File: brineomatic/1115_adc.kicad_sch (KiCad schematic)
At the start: 4 parts, among them U1 ADS1015IDGS

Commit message: getting closer.  added tds
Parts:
- removed U1: ADS1015IDGS, Package_SO:TSSOP-10_3x3mm_P0.5mm, symbol Analog_ADC:ADS1015IDGS
- added R20, R21: 2.2k, Resistor_SMD:R_0805_2012Metric_Pad1.20x1.40mm_HandSolder, symbol Device:R_Small_US
- added U6: ADS1115IDGS, Package_SO:TSSOP-10_3x3mm_P0.5mm, symbol Analog_ADC:ADS1115IDGS
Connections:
- net +3.3V: now also R20.2, R21.2, U6.8 (VDD)
- net ADC0: now also U6.4 (AIN0)
- net ADC1: now also U6.5 (AIN1)
- net ADC2: now also U6.6 (AIN2)
- net ADC3: now also U6.7 (AIN3)
- net ADDR: now also U6.1 (ADDR)
- net SCL: now also R20.1, U6.10 (SCL)
- net SDA: now also R21.1, U6.9 (SDA)
- net at R14.1: now also U6.2 (ALERT/RDY)
- net GNDA renamed GND
- net GND: now also U6.3 (GND)
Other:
- moved on the sheet: C4, C5

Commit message: starting to shape up, footprints etc
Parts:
- renumbered C4 to C7, C5 to C8, R20 to R15, R21 to R16, U6 to U3
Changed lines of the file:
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@@
 		(on_board yes)
 		(dnp no)
-		(property "Reference" "C4"
+		(property "Reference" "C7"
 			(at 184.15 80.0163 0)
 			(effects
@@
 			(project "brineomatic"
 				(path "/96477ae2-ef08-48f3-8dd4-fe4478541f68/64f85b9c-b5dc-4ec9-9075-ce977ed1cba6"
-					(reference "C4")
+					(reference "C7")
 					(unit 1)
 				)
@@
 		(on_board yes)
 		(dnp no)
-		(property "Reference" "C5"
+		(property "Reference" "C8"
 			(at 195.58 80.0163 0)
 			(effects
@@
 			(project "brineomatic"
 				(path "/96477ae2-ef08-48f3-8dd4-fe4478541f68/64f85b9c-b5dc-4ec9-9075-ce977ed1cba6"
-					(reference "C5")
+					(reference "C8")
 					(unit 1)
 				)
@@
 		(dnp no)
 		(fields_autoplaced yes)
-		(property "Reference" "#PWR014"
+		(property "Reference" "#PWR020"
 			(at 127 69.85 0)
 			(effects
@@
 			(project "brineomatic"
 				(path "/96477ae2-ef08-48f3-8dd4-fe4478541f68/64f85b9c-b5dc-4ec9-9075-ce977ed1cba6"
-					(reference "#PWR014")
+					(reference "#PWR020")
 					(unit 1)
 				)
@@
 		(dnp no)
 		(fields_autoplaced yes)
-		(property "Reference" "R20"
+		(property "Reference" "R15"
 			(at 157.48 80.01 0)
 			(effects
@@
 			(project "brineomatic"
 				(path "/96477ae2-ef08-48f3-8dd4-fe4478541f68/64f85b9c-b5dc-4ec9-9075-ce977ed1cba6"
-					(reference "R20")
+					(reference "R15")
 					(unit 1)
 				)
@@
 		(dnp no)
 		(fields_autoplaced yes)
-		(property "Reference" "U6"
+		(property "Reference" "U3"
 			(at 129.1941 71.12 0)
 			(effects
@@
 			(project ""
 				(path "/96477ae2-ef08-48f3-8dd4-fe4478541f68/64f85b9c-b5dc-4ec9-9075-ce977ed1cba6"
-					(reference "U6")
+					(reference "U3")
 					(unit 1)
 				)
@@
 		(dnp no)
 		(fields_autoplaced yes)
-		(property "Reference" "#PWR015"
+		(property "Reference" "#PWR021"
 			(at 127 105.41 0)
 			(effects
@@
 			(project ""
 				(path "/96477ae2-ef08-48f3-8dd4-fe4478541f68/64f85b9c-b5dc-4ec9-9075-ce977ed1cba6"
-					(reference "#PWR015")
+					(reference "#PWR021")
 					(unit 1)
 				)
@@
 		(dnp no)
 		(fields_autoplaced yes)
-		(property "Reference" "R21"
+		(property "Reference" "R16"
 			(at 167.64 80.01 0)
 			(effects
@@
 			(project "brineomatic"
 				(path "/96477ae2-ef08-48f3-8dd4-fe4478541f68/64f85b9c-b5dc-4ec9-9075-ce977ed1cba6"
-					(reference "R21")
-					(unit 1)
-				)
+					(reference "R16")
+					(unit 1)
+				)

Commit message: updated bom and prepping for Rev A
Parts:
- R14: value 10k -> 10K
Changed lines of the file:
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@@
 			)
 		)
-		(property "Value" "10k"
+		(property "Value" "10K"
 			(at 148.59 74.93 0)
 			(effects

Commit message: updates parts, footprints, etc.  ready for production.
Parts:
- U3: value ADS1115IDGS -> ADS1115IDGSR; LCSC C37593 -> (none); Mouser (none) -> 595-ADS1115IDGSR
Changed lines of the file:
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@@
 			)
 		)
-		(property "Value" "ADS1115IDGS"
+		(property "Value" "ADS1115IDGSR"
 			(at 129.1941 73.66 0)
 			(effects
@@
 			)
 		)
-		(property "LCSC" "C37593"
+		(property "LCSC" ""
 			(at 127 86.36 0)
 			(effects
+				(font
+					(size 1.27 1.27)
+				)
+				(hide yes)
+			)
+		)
+		(property "Mouser" " 595-ADS1115IDGSR "
+			(at 127 86.36 0)
+			(effects

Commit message: added alert line to adc
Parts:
- removed R14: 10K, Resistor_SMD:R_0805_2012Metric_Pad1.20x1.40mm_HandSolder, symbol Device:R_Small_US
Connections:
- net ALERT/RDY: now reaches U3.2 (ALERT/RDY)
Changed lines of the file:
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@@
-	)
-	(junction
-		(at 146.05 67.31)
-		(diameter 0)
-		(color 0 0 0 0)
 	)
 	(junction
@@
 	(wire
 		(pts
-			(xy 146.05 67.31) (xy 154.94 67.31)
-		)
-		(stroke
-			(width 0)
-			(type default)
-		)
-	)
-	(wire
-		(pts
 			(xy 127 96.52) (xy 127 97.79)
 		)
@@
 	(wire
 		(pts
-			(xy 127 67.31) (xy 146.05 67.31)
+			(xy 127 67.31) (xy 154.94 67.31)
 		)
 		(stroke
@@
 	(wire
 		(pts
-			(xy 146.05 67.31) (xy 146.05 71.12)
-		)
-		(stroke
-			(width 0)
-			(type default)
-		)
-	)
-	(wire
-		(pts
 			(xy 154.94 67.31) (xy 165.1 67.31)
 		)
@@
 	(wire
 		(pts
-			(xy 146.05 81.28) (xy 146.05 76.2)
-		)
-		(stroke
-			(width 0)
-			(type default)
-		)
-	)
-	(wire
-		(pts
 			(xy 137.16 91.44) (xy 140.97 91.44)
 		)
@@
 	(wire
 		(pts
-			(xy 137.16 81.28) (xy 146.05 81.28)
+			(xy 137.16 81.28) (xy 140.97 81.28)
 		)
 		(stroke
@@
 		(shape input)
 		(at 140.97 91.44 0)
+		(fields_autoplaced yes)
+		(effects
+			(font
+				(size 1.27 1.27)
+			)
+			(justify left)
+		)
+	)
+	(hierarchical_label "ALERT{slash}RDY"
+		(shape input)
+		(at 140.97 81.28 0)
 		(fields_autoplaced yes)
 		(effects
@@
 					(unit 1)
 				)
-			)
-		)
-	)
-	(symbol
-		(lib_id "Device:R_Small_US")
-		(at 146.05 73.66 180)
-		(unit 1)
-		(exclude_from_sim no)
-		(in_bom yes)
-		(on_board yes)
-		(dnp no)
-		(fields_autoplaced yes)
-		(property "Reference" "R14"
-			(at 148.59 72.39 0)
-			(effects
-				(font
-					(size 1.27 1.27)
-				)
-				(justify right)
-			)
-		)
-		(property "Value" "10K"
-			(at 148.59 74.93 0)
-			(effects
-				(font
-					(size 1.27 1.27)
-				)
-				(justify right)
-			)
-		)
-		(property "Footprint" "Resistor_SMD:R_0805_2012Metric_Pad1.20x1.40mm_HandSolder"
-			(at 146.05 73.66 0)
-			(effects
-				(font
-					(size 1.27 1.27)
-				)
-				(hide yes)
-			)
-		)
-		(property "Datasheet" "~"
-			(at 146.05 73.66 0)
-			(effects
-				(font
-					(size 1.27 1.27)
-				)
-				(hide yes)
-			)
-		)
-		(property "Description" ""
-			(at 146.05 73.66 0)
-			(effects
-				(font
-					(size 1.27 1.27)
-				)
-				(hide yes)
-			)
-		)
-		(property "LCSC" "C84376"
-			(at 146.05 73.66 0)
-			(effects
-				(font
-					(size 1.27 1.27)
-				)
-				(hide yes)
-			)
-		)
-		(pin "1"
-		)
-		(pin "2"
-		)
-		(instances
-			(project "brineomatic"
-				(path "/96477ae2-ef08-48f3-8dd4-fe4478541f68/64f85b9c-b5dc-4ec9-9075-ce977ed1cba6"
-					(reference "R14")
-					(unit 1)
-				)

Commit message: worked on schematic and layout a bit more.
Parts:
- C7, C8: footprint Capacitor_SMD:C_0805_2012Metric_Pad1.18x1.45mm_HandSolder -> Capacitor_SMD:C_0603_1608Metric
- R15, R16: footprint Resistor_SMD:R_0805_2012Metric_Pad1.20x1.40mm_HandSolder -> Resistor_SMD:R_0603_1608Metric
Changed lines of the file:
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@@
 			)
 		)
-		(property "Footprint" "Capacitor_SMD:C_0805_2012Metric_Pad1.18x1.45mm_HandSolder"
+		(property "Footprint" "Capacitor_SMD:C_0603_1608Metric"
 			(at 181.61 81.28 0)
 			(effects
@@
 			)
 		)
-		(property "Footprint" "Capacitor_SMD:C_0805_2012Metric_Pad1.18x1.45mm_HandSolder"
+		(property "Footprint" "Capacitor_SMD:C_0603_1608Metric"
 			(at 193.04 81.28 0)
 			(effects
@@
 			)
 		)
-		(property "Footprint" "Resistor_SMD:R_0805_2012Metric_Pad1.20x1.40mm_HandSolder"
+		(property "Footprint" "Resistor_SMD:R_0603_1608Metric"
 			(at 154.94 81.28 0)
 			(effects
@@
 			)
 		)
-		(property "Footprint" "Resistor_SMD:R_0805_2012Metric_Pad1.20x1.40mm_HandSolder"
+		(property "Footprint" "Resistor_SMD:R_0603_1608Metric"
 			(at 165.1 81.28 0)
 			(effects

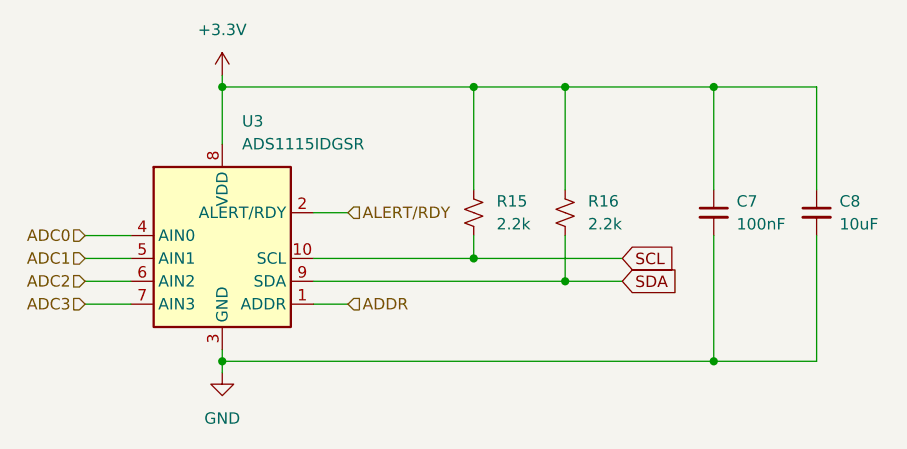
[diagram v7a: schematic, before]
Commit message: switched to onboard esp32-s3 and re-drew tmc2209 driver
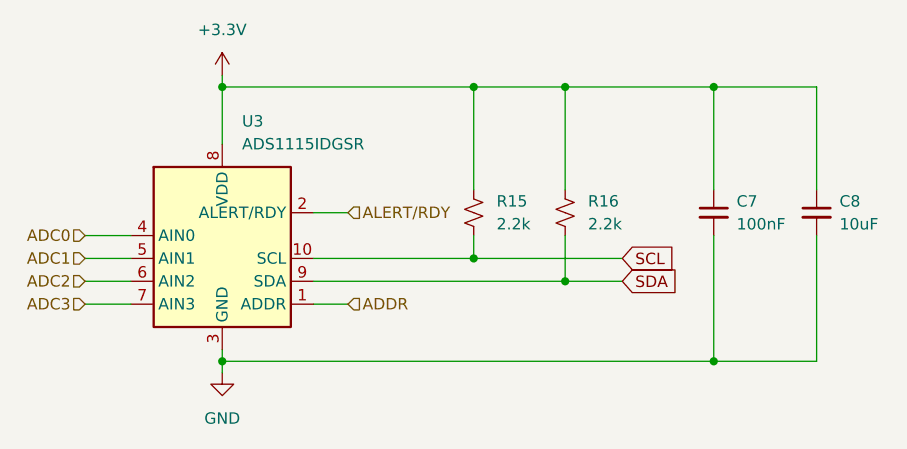
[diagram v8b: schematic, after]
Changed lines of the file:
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@@
 		(fields_autoplaced yes)
 		(property "Reference" "R15"
-			(at 157.48 80.01 0)
+			(at 157.48 80.0099 0)
 			(effects
 				(font
@@
 		)
 		(property "Value" "2.2k"
-			(at 157.48 82.55 0)
+			(at 157.48 82.5499 0)
 			(effects
 				(font
@@
 			)
 		)
-		(property "Description" ""
+		(property "Description" "Resistor, small US symbol"
 			(at 154.94 81.28 0)
 			(effects
@@
 		(fields_autoplaced yes)
 		(property "Reference" "R16"
-			(at 167.64 80.01 0)
+			(at 167.64 80.0099 0)
 			(effects
 				(font
@@
 		)
 		(property "Value" "2.2k"
-			(at 167.64 82.55 0)
+			(at 167.64 82.5499 0)
 			(effects
 				(font
@@
 			)
 		)
-		(property "Description" ""
+		(property "Description" "Resistor, small US symbol"
 			(at 165.1 81.28 0)
 			(effects
